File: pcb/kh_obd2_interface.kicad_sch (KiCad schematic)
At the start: 0 parts

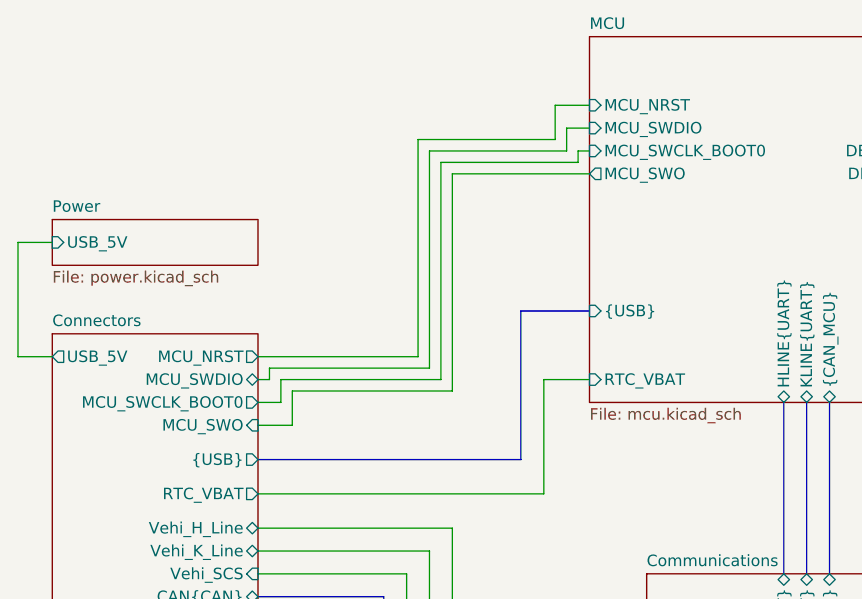
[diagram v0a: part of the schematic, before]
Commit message: fix CAN tx/rx/stb, remove unused SWO
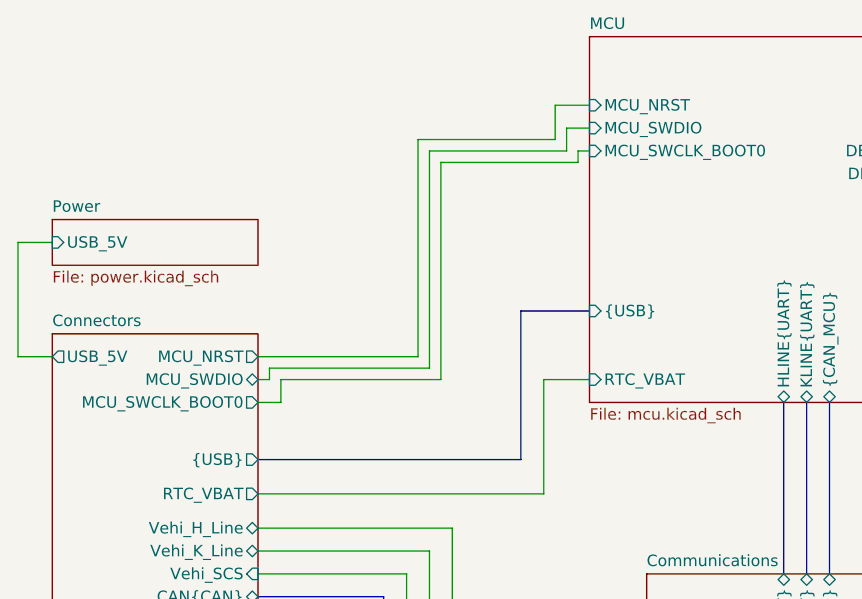
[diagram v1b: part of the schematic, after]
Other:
- sheet Connectors ports: added none; removed MCU_SWO
- sheet MCU ports: added none; removed MCU_SWO
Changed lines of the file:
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@@
-		)
-	)
-	(wire
-		(pts
-			(xy 96.52 44.45) (xy 111.76 44.45)
-		)
-		(stroke
-			(width 0)
-			(type default)
 		)
 	)
@@
 	(wire
 		(pts
-			(xy 78.74 68.58) (xy 78.74 72.39)
-		)
-		(stroke
-			(width 0)
-			(type default)
-		)
-	)
-	(wire
-		(pts
 			(xy 74.93 80.01) (xy 106.68 80.01)
 		)
@@
 	(wire
 		(pts
-			(xy 96.52 44.45) (xy 96.52 68.58)
-		)
-		(stroke
-			(width 0)
-			(type default)
-		)
-	)
-	(wire
-		(pts
 			(xy 74.93 83.82) (xy 96.52 83.82)
 		)
@@
 	(wire
 		(pts
-			(xy 78.74 72.39) (xy 74.93 72.39)
-		)
-		(stroke
-			(width 0)
-			(type default)
-		)
-	)
-	(wire
-		(pts
 			(xy 93.98 86.36) (xy 93.98 95.25)
 		)
@@
 		(pts
 			(xy 48.26 64.77) (xy 52.07 64.77)
-		)
-		(stroke
-			(width 0)
-			(type default)
-		)
-	)
-	(wire
-		(pts
-			(xy 78.74 68.58) (xy 96.52 68.58)
 		)
 		(stroke
@@
 			)
 		)
-		(pin "MCU_SWO" input
-			(at 74.93 72.39 0)
-			(effects
-				(font
-					(size 1.27 1.27)
-				)
-				(justify right)
-			)
-		)
 		(pin "USB_5V" output
 			(at 52.07 64.77 180)
@@
 			)
 		)
-		(pin "MCU_SWO" output
-			(at 111.76 44.45 180)
-			(effects
-				(font
-					(size 1.27 1.27)
-				)
-				(justify left)
-			)
-		)

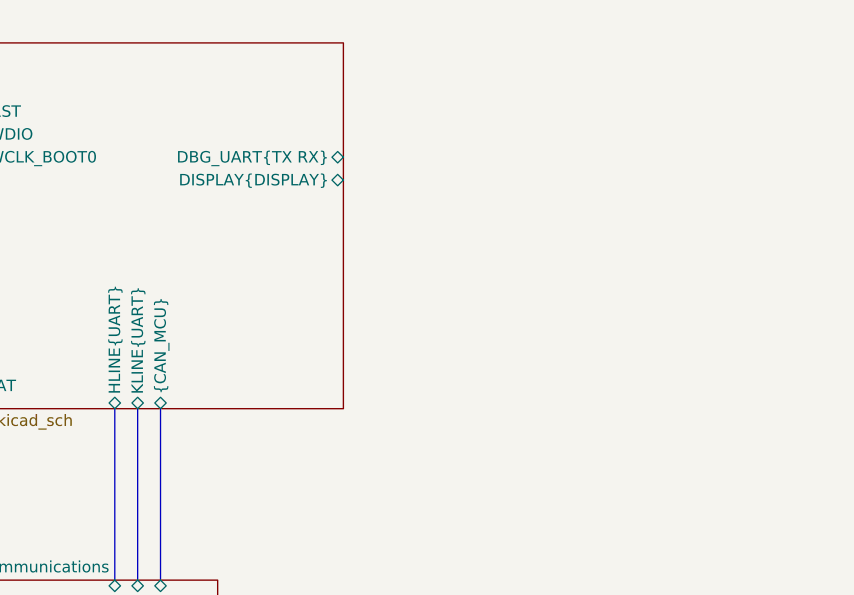
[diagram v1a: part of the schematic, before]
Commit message: status/info leds, extra 5v cap
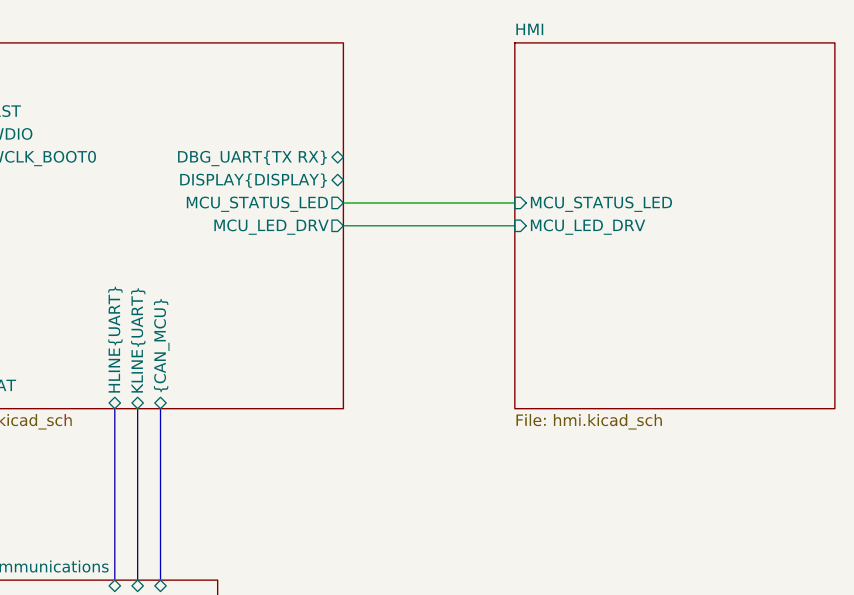
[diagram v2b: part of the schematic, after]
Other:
- added sheet HMI (hmi.kicad_sch)
- sheet MCU ports: added MCU_LED_DRV, MCU_STATUS_LED; removed none
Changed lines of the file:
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@@
+	(wire
+		(pts
+			(xy 158.75 49.53) (xy 177.8 49.53)
+		)
+		(stroke
+			(width 0)
+			(type default)
+		)
+	)
 	(wire
 		(pts
@@
 		(pts
 			(xy 109.22 39.37) (xy 111.76 39.37)
+		)
+		(stroke
+			(width 0)
+			(type default)
+		)
+	)
+	(wire
+		(pts
+			(xy 158.75 46.99) (xy 177.8 46.99)
 		)
 		(stroke
@@
 			(project "kh_obd2_interface"
 				(path "/0736e313-8db4-41af-b70d-53af7104d2ca"
-					(page "5")
+					(page "4")
 				)
 			)
@@
 			(project "kh_obd2_interface"
 				(path "/0736e313-8db4-41af-b70d-53af7104d2ca"
-					(page "3")
+					(page "1")
 				)
 			)
@@
 			(project "kh_obd2_interface"
 				(path "/0736e313-8db4-41af-b70d-53af7104d2ca"
-					(page "4")
+					(page "3")
 				)
 			)
@@
 			)
 		)
+		(pin "MCU_STATUS_LED" output
+			(at 158.75 46.99 0)
+			(effects
+				(font
+					(size 1.27 1.27)
+				)
+				(justify right)
+			)
+		)
+		(pin "MCU_LED_DRV" output
+			(at 158.75 49.53 0)
+			(effects
+				(font
+					(size 1.27 1.27)
+				)
+				(justify right)
+			)
+		)
 		(instances
 			(project "kh_obd2_interface"
@@
 		)
 	)
+	(sheet
+		(at 177.8 29.21)
+		(size 35.56 40.64)
+		(exclude_from_sim no)
+		(in_bom yes)
+		(on_board yes)
+		(dnp no)
+		(fields_autoplaced yes)
+		(stroke
+			(width 0.1524)
+			(type solid)
+		)
+		(fill
+			(color 0 0 0 0.0000)
+		)
+		(property "Sheetname" "HMI"
+			(at 177.8 28.4984 0)
+			(effects
+				(font
+					(size 1.27 1.27)
+				)
+				(justify left bottom)
+			)
+		)
+		(property "Sheetfile" "hmi.kicad_sch"
+			(at 177.8 70.4346 0)
+			(effects
+				(font
+					(size 1.27 1.27)
+				)
+				(justify left top)
+			)
+		)
+		(pin "MCU_STATUS_LED" input
+			(at 177.8 46.99 180)
+			(effects
+				(font
+					(size 1.27 1.27)
+				)
+				(justify left)
+			)
+		)
+		(pin "MCU_LED_DRV" input
+			(at 177.8 49.53 180)
+			(effects
+				(font
+					(size 1.27 1.27)
+				)
+				(justify left)
+			)
+		)
+		(instances
+			(project "kh_obd2_interface"
+				(path "/0736e313-8db4-41af-b70d-53af7104d2ca"
+					(page "5")
+				)
+			)
+		)
+	)
 	(sheet_instances
 		(path "/"
-			(page "1")
-		)
-	)
+			(page "0")
+		)
+	)

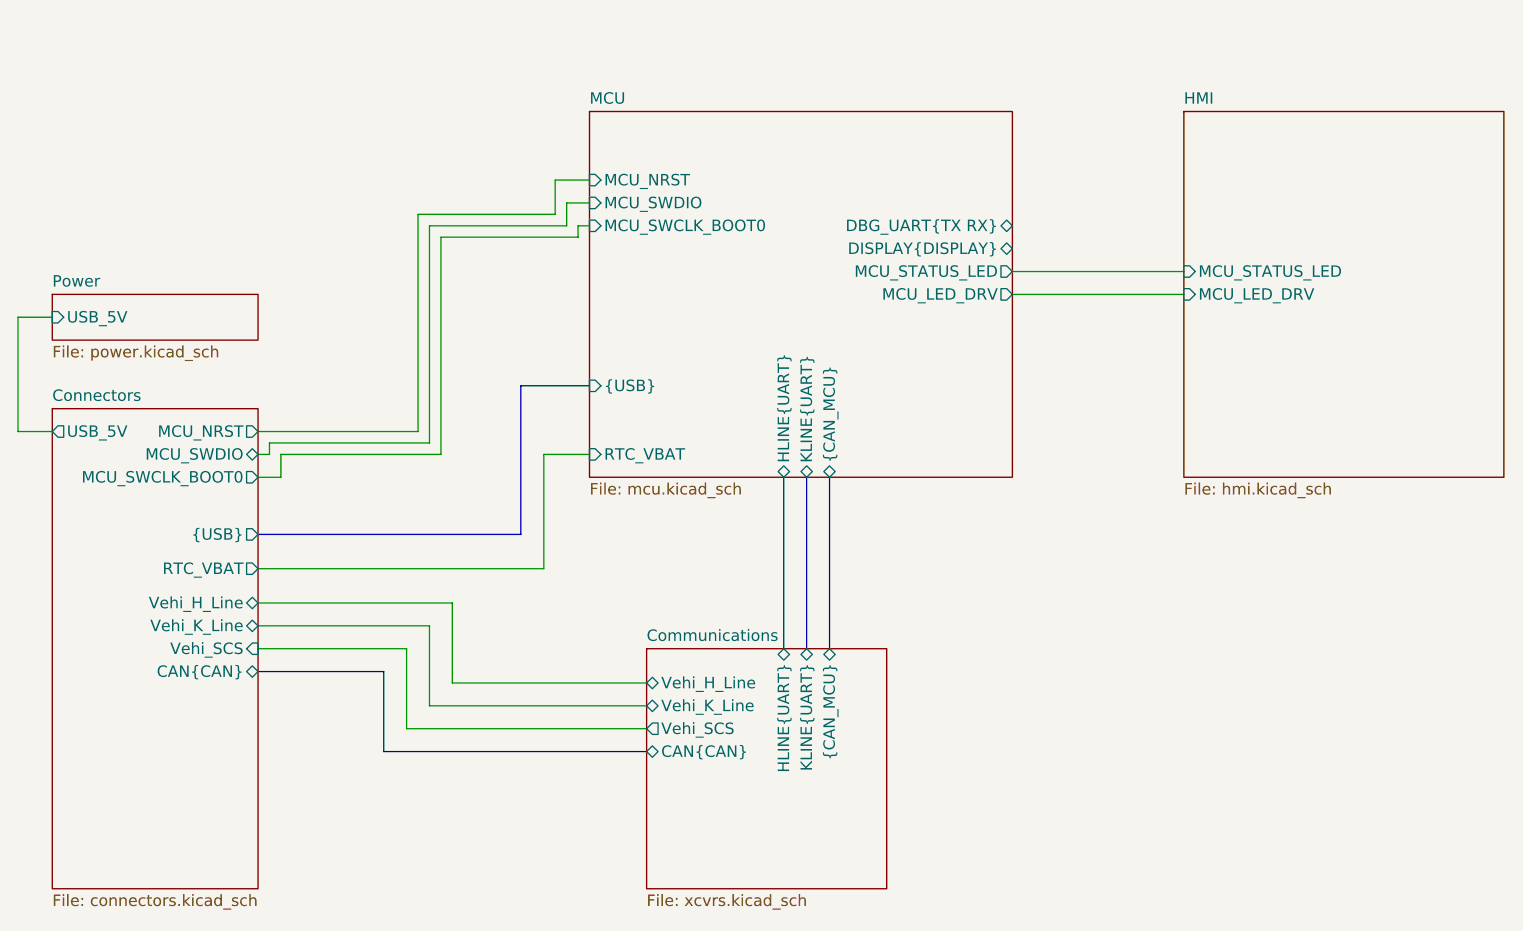
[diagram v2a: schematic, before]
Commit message: dbg uart, nrst, SCS drive, etc
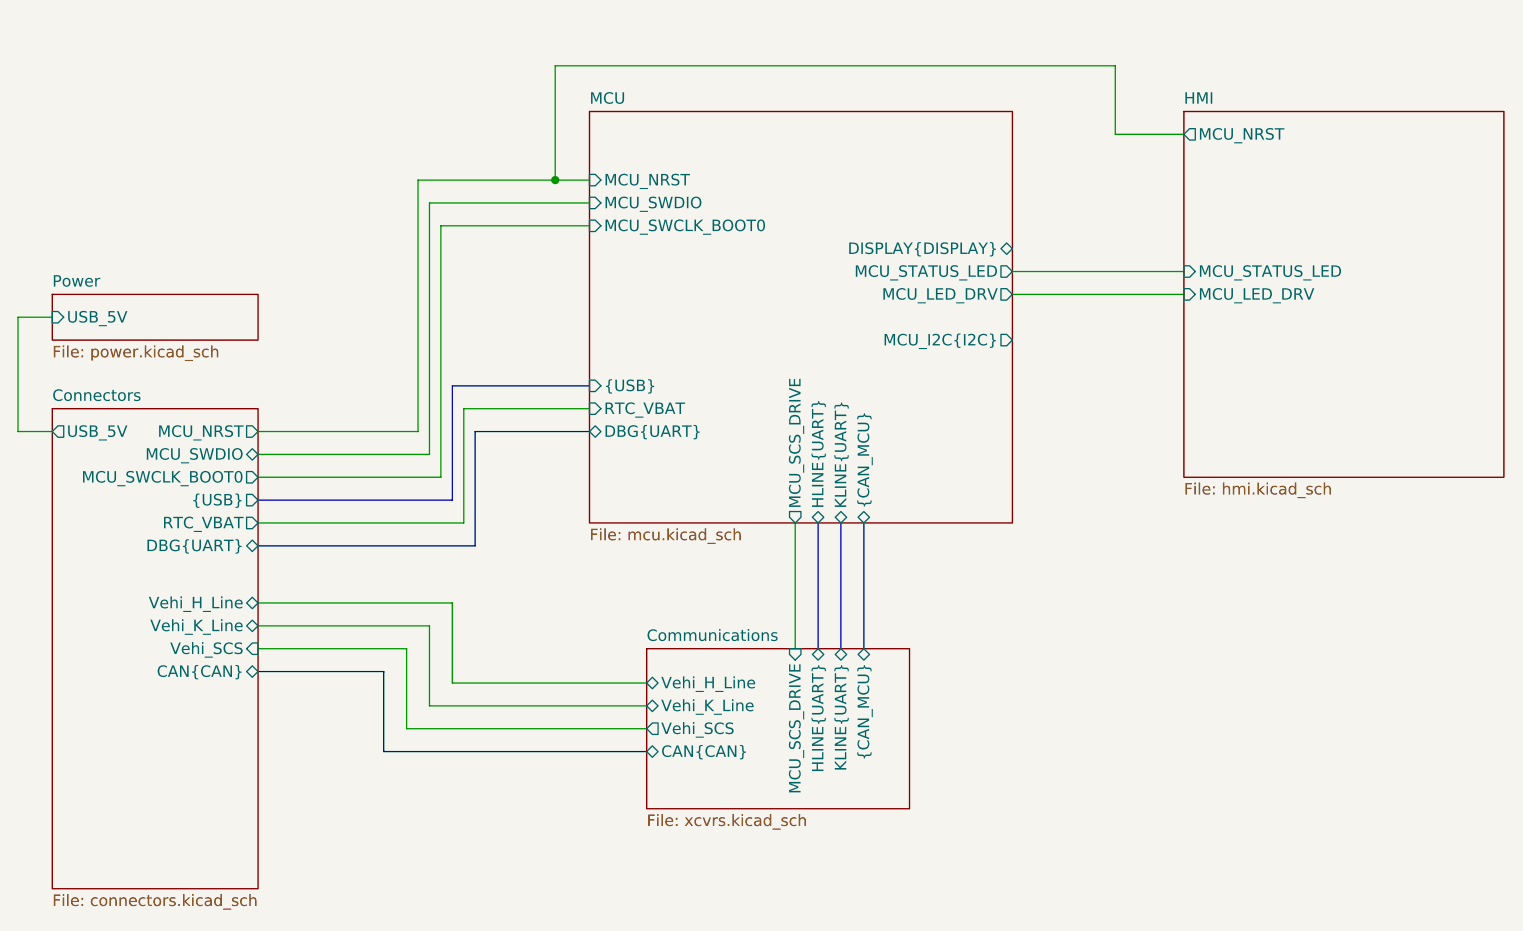
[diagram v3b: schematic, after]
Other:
- sheet Communications ports: added MCU_SCS_DRIVE; removed none
- sheet Connectors ports: added DBG{UART}; removed none
- sheet HMI ports: added MCU_NRST; removed none
- sheet MCU ports: added DBG{UART}, MCU_I2C{I2C}, MCU_SCS_DRIVE; removed DBG_UART{TX RX}

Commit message: connector prep
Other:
- sheet MCU ports: added MCU_DISPLAY{DISPLAY}; removed DISPLAY{DISPLAY}
